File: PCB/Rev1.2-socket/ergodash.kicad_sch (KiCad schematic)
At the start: 183 parts, among them J1 5PIN, J2 Conn_01x03, J3 Conn_01x03, J4 GS3, J5 GS3, M1 Speaker, Q1 IRLML6344TRPbF, SW1 SW_PUSH, SW10 SW_PUSH, SW11 SW_PUSH, SW12 SW_PUSH, SW13 SW_PUSH, SW14 SW_PUSH, SW15 SW_PUSH, SW16 SW_PUSH, SW17 SW_PUSH, SW18 SW_PUSH, SW19 SW_PUSH, SW2 SW_PUSH, SW20 SW_PUSH, SW21 SW_PUSH, SW22 SW_PUSH, SW23 SW_PUSH, SW24 SW_PUSH, SW25 SW_PUSH, SW26 SW_PUSH, SW27 SW_PUSH, SW28 SW_PUSH, SW29 SW_Push, SW3 SW_PUSH, SW30 SW_PUSH, SW31 SW_PUSH, SW32 SW_PUSH, SW33 SW_PUSH, SW34 SW_PUSH, SW35 SW_PUSH, SW36 SW_PUSH, SW37 SW_Push, SW38 SW_PUSH, SW39 SW_PUSH, SW4 SW_PUSH, SW40 SW_PUSH, SW41 SW_PUSH, SW5 SW_PUSH, SW6 SW_PUSH, SW7 SW_PUSH, SW8 SW_PUSH, SW9 SW_PUSH, U1 HOLE, U2 HOLE, U3 ProMicro, U4 HOLE, U5 HOLE, U6 ProMicro, U7 HOLE, U8 HOLE, U9 HOLE

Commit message: Fix broken symbol resolution in KiCad 10 conversion
The first conversion silently dropped every custom symbol
(SW_PUSH, ProMicro, WS2812B, connectors, ...) because the legacy
schematic references libraries by their original nicknames while
KiCad only registered the cache library as ergodash-cache,
leaving those symbols pinless and disconnecting the switch matrix,
GND and more.

Split ergodash-cache.lib into per-nickname libraries under
library/ and register them in sym-lib-table, then re-import the
schematic. The exported netlist now matches the original
Rev1.2 netlist exactly (all 111 nets identical in membership).
Drop the legacy source files again now that the conversion is
verified.

Co-Authored-By: Claude Fable 5 <noreply@anthropic.com>
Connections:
- net Audio: now also U3.8 (C6), U6.8 (C6)
- net Backlight: now also U3.13 (B6), U6.13 (B6)
- net GND: now also J1.4, J1.5, J2.3 (Pin_3), J3.3 (Pin_3), J4.3 (G3), J5.3 (G3), M1.1 (GND), Q1.2 (S), SW29.2, SW37.2, U3.23 (GND), U3.3 (GND), U3.4 (GND), U6.23 (GND), U6.3 (GND), U6.4 (GND)
- net RBG: now also J2.2 (Pin_2), LED1.2 (DOUT), U3.1 (TX), U6.1 (TX)
- net RX: now also U3.2 (RX), U6.2 (RX)
- net VCC: now also J1.1, J2.1 (Pin_1), J3.1 (Pin_1), J4.1 (G1), J5.1 (G1), U3.21 (VCC), U6.21 (VCC)
- net col0: now also SW1.1, SW2.1, SW3.1, SW30.1, SW4.1, U3.20 (F4), U6.20 (F4)
- net col1: now also SW31.1, SW5.1, SW6.1, SW7.1, SW8.1, U3.19 (F5), U6.19 (F5)
- net col2: now also SW10.1, SW11.1, SW12.1, SW32.1, SW9.1, U3.18 (F6), U6.18 (F6)
- net col3: now also SW13.1, SW14.1, SW15.1, SW16.1, SW33.1, SW38.1, U3.17 (F7), U6.17 (F7)
- net col4: now also SW17.1, SW18.1, SW19.1, SW20.1, SW34.1, U3.16 (B1), U6.16 (B1)
- net col5: now also SW21.1, SW22.1, SW23.1, SW24.1, SW35.1, SW36.1, U3.15 (B3), U6.15 (B3)
- net col6: now also SW25.1, SW26.1, SW27.1, SW28.1, SW39.1, SW40.1, SW41.1, U3.14 (B2), U6.14 (B2)
- net row0: now also U3.7 (D4), U6.7 (D4)
- net row1: now also U3.9 (D7), U6.9 (D7)
- net row2: now also U3.10 (E6), U6.10 (E6)
- net row3: now also U3.11 (B4), U6.11 (B4)
- net row4: now also U3.12 (B5), U6.12 (B5)
- net rst: now also SW29.1, SW37.1, U3.22 (RST), U6.22 (RST)
- net scl: now also U3.5 (SCL), U6.5 (SCL), W1.2
- net sda/uart: now also J1.3, U3.6 (SDA), U6.6 (SDA)
- net xtradata: now also J1.2, J3.2 (Pin_2), LED12.4 (DIN), W1.1
- net at D1.2 (A): now also SW1.2
- net at D5.2 (A): now also SW5.2
- net at D9.2 (A): now also SW9.2
- net at D13.2 (A): now also SW13.2
- net at D17.2 (A): now also SW17.2
- net at D21.2 (A): now also SW21.2
- net at D25.2 (A): now also SW25.2
- net at D2.2 (A): now also SW2.2
- net at D6.2 (A): now also SW6.2
- net at D10.2 (A): now also SW10.2
- net at D14.2 (A): now also SW14.2
- net at D18.2 (A): now also SW18.2
- net at D22.2 (A): now also SW22.2
- net at D26.2 (A): now also SW26.2
- net at D27.2 (A): now also SW27.2
- net at D23.2 (A): now also SW23.2
- net at D19.2 (A): now also SW19.2
- net at D15.2 (A): now also SW15.2
- net at D11.2 (A): now also SW11.2
- net at D7.2 (A): now also SW7.2
- net at D3.2 (A): now also SW3.2
- net at D4.2 (A): now also SW4.2
- net at D8.2 (A): now also SW8.2
- net at D12.2 (A): now also SW12.2
- net at D16.2 (A): now also SW16.2
- net at D20.2 (A): now also SW20.2
- net at D24.2 (A): now also SW24.2
- net at D28.2 (A): now also SW28.2, SW39.2
- net at D29.2 (A): now also SW30.2
- net at D30.2 (A): now also SW31.2
- net at D31.2 (A): now also SW32.2
- net at D32.2 (A): now also SW33.2, SW38.2
- net at D33.2 (A): now also SW34.2
- net at D34.2 (A): now also SW35.2, SW36.2
- net at R10.2, R11.2, R12.2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: now also Q1.3 (D)
- net at R13.2: now also Q1.1 (G)
- net at D68.2 (A): now also SW40.2, SW41.2
- net at R40.2: now also M1.2 (Audio)
- new net: J4.2 (G2), LED1.1 (VCC), LED10.1 (VCC), LED11.1 (VCC), LED12.1 (VCC), LED2.1 (VCC), LED3.1 (VCC), LED4.1 (VCC), LED5.1 (VCC), LED6.1 (VCC), LED7.1 (VCC), LED8.1 (VCC), LED9.1 (VCC)
- new net: J5.2 (G2), LED1.3 (GND), LED10.3 (GND), LED11.3 (GND), LED12.3 (GND), LED2.3 (GND), LED3.3 (GND), LED4.3 (GND), LED5.3 (GND), LED6.3 (GND), LED7.3 (GND), LED8.3 (GND), LED9.3 (GND)
- new net: LED1.4 (DIN), LED2.2 (DOUT)
- new net: LED2.4 (DIN), LED3.2 (DOUT)
- new net: LED3.4 (DIN), LED4.2 (DOUT)
- new net: LED4.4 (DIN), LED5.2 (DOUT)
- new net: LED5.4 (DIN), LED6.2 (DOUT)
- new net: LED6.4 (DIN), LED7.2 (DOUT)
- new net: LED7.4 (DIN), LED8.2 (DOUT)
- new net: LED8.4 (DIN), LED9.2 (DOUT)
- new net: LED10.2 (DOUT), LED9.4 (DIN)
- new net: LED10.4 (DIN), LED11.2 (DOUT)
- new net: LED11.4 (DIN), LED12.2 (DOUT)

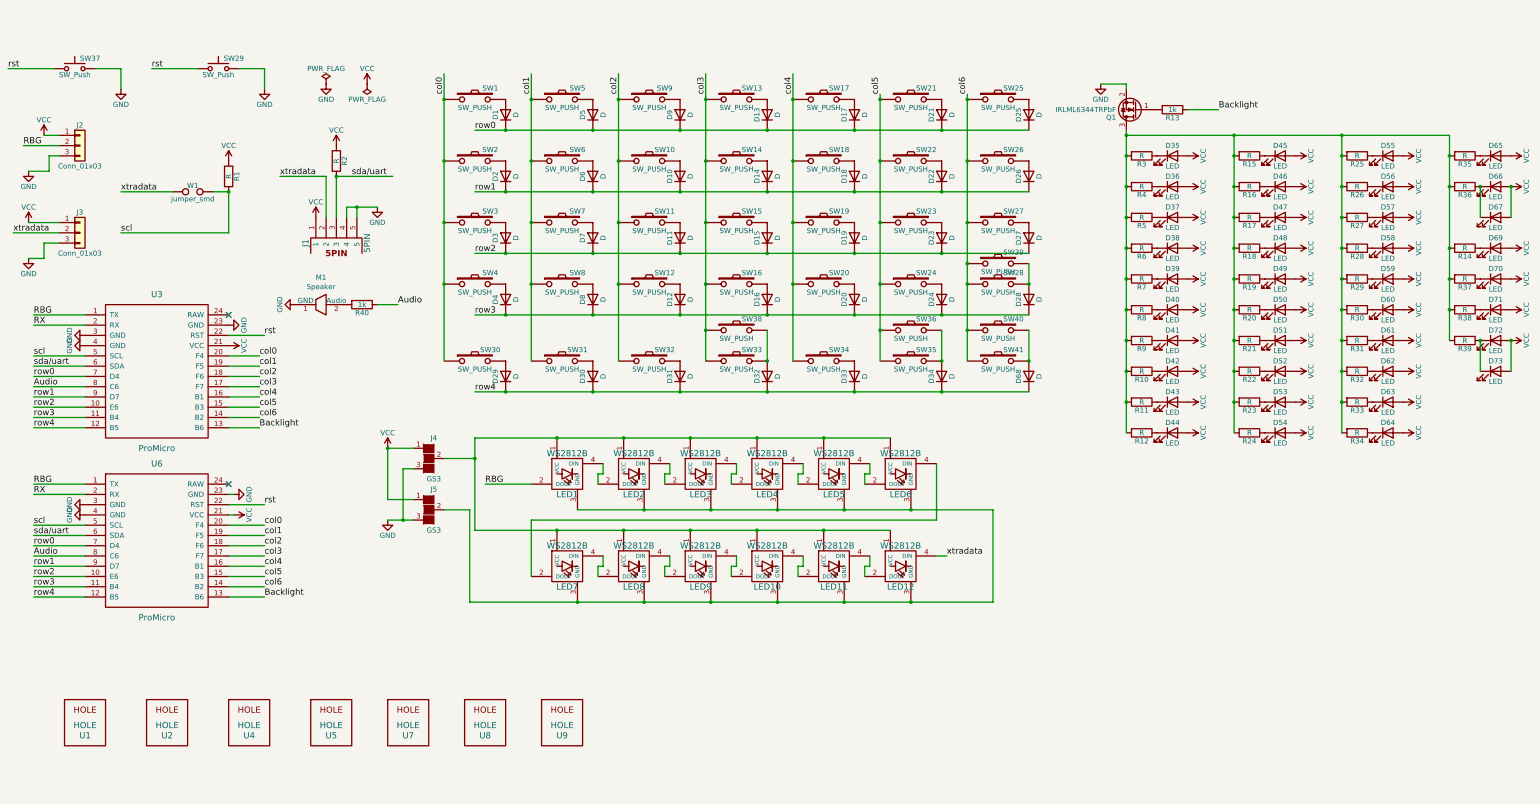
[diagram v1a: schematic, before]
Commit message: Remove all LED options from the schematic
Per the socket-version design policy: delete the WS2812B underglow
chain (LED1-12), per-switch 3mm backlight LEDs (D35-D67, D69-D73),
their 470 ohm resistors (R3-R12, R14-R39), the backlight driver
(Q1, R13) and the LED connectors/jumpers (J2-J5).

Verified by netlist diff against upstream Rev1.2: all 55 remaining
key-matrix/power/TRRS nets are identical in membership; the only
removed nets are LED-related. D68 (row4 matrix diode) and xtradata
(TRRS extra line) are intact.

Co-Authored-By: Claude Fable 5 <noreply@anthropic.com>
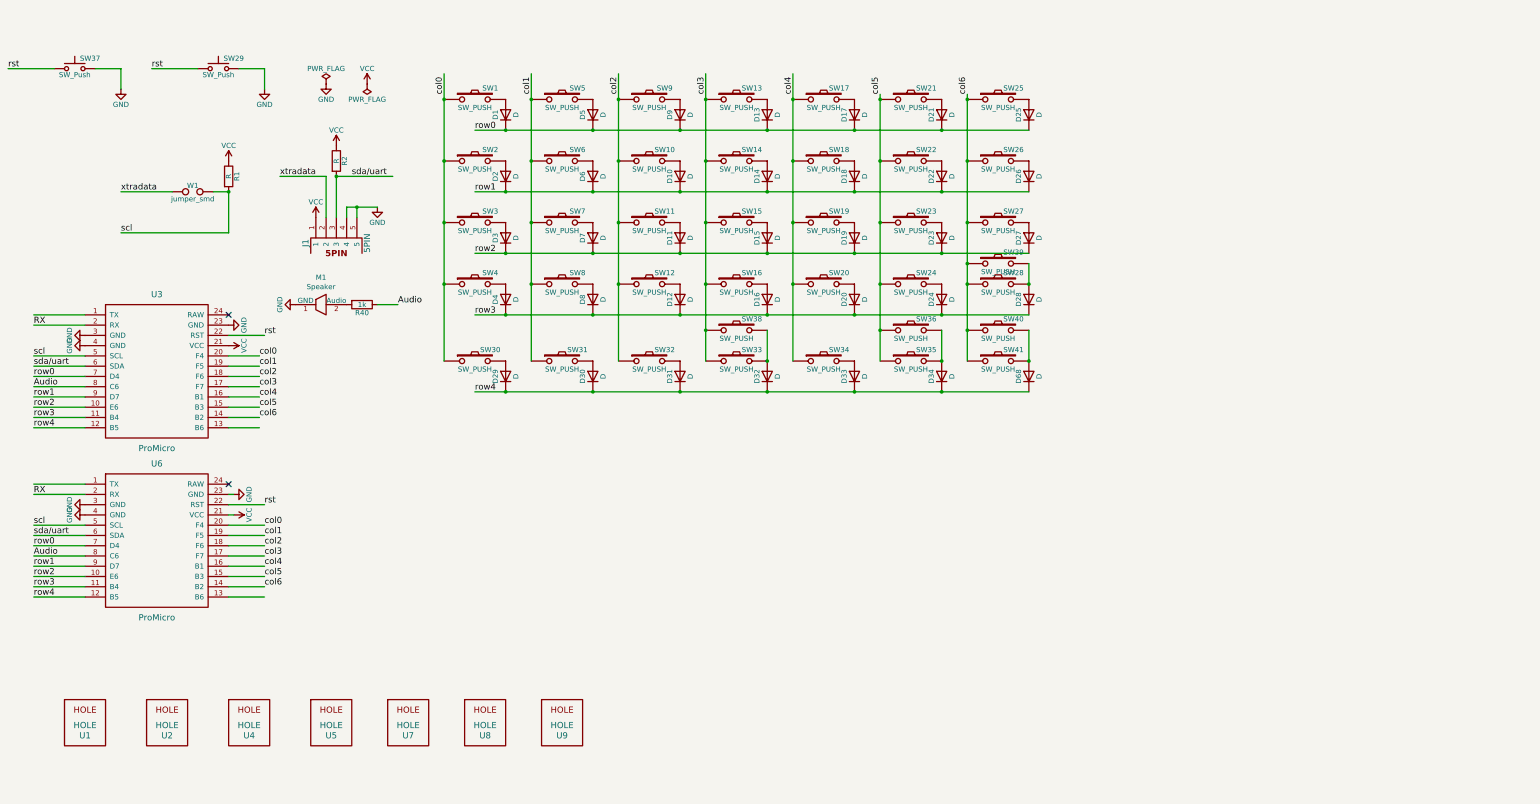
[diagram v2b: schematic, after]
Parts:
- removed D35, D36, D37, D38, D39, D40, D41, D42, D43, D44, D45, D46, D47, D48, D49, D50, D51, D52, D53, D54, D55, D56, D57, D58, D59, D60, D61, D62, D63, D64, D65, D66, D67, D69, D70, D71, D72, D73: LED, library:CHERRY_MX_LED2, symbol Device:LED
- removed J2, J3: Conn_01x03, library:conn3, symbol conn:Conn_01x03
- removed J4, J5: GS3, library:jumper2, symbol conn:GS3
- removed LED1, LED10, LED11, LED12, LED2, LED3, LED4, LED5, LED6, LED7, LED8, LED9: WS2812B, library:WS2812B-5, symbol ws2812b:WS2812B
- removed Q1: IRLML6344TRPbF, library:SOT-23_2, symbol transistors:BSS138
- removed R10, R11, R12, R14, R15, R16, R17, R18, R19, R20, R21, R22, R23, R24, R25, R26, R27, R28, R29, R3, R30, R31, R32, R33, R34, R35, R36, R37, R38, R39, R4, R5, R6, R7, R8, R9: R, library:Resistors_SMD_THT, symbol Device:R
- removed R13: 1k, library:Resistors_SMD_THT, symbol Device:R
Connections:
- net Backlight: no longer names the net of U3.13 (B6)
- net Backlight: no longer U6.13 (B6)
- net RBG: no longer names the net of U3.1 (TX)
- net RBG: no longer U6.1 (TX)

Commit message: Assign Kailh hotswap socket footprint to all key switches
Point the 39 SW_PUSH symbols at socket:SW_Hotswap_Kailh_MX_Plated
and fix the TRRS jack footprint reference to match the footprint
actually used on the board (trrs_jack2). Netlist unchanged.

Co-Authored-By: Claude Fable 5 <noreply@anthropic.com>
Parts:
- J1: footprint library:trrs_jack -> library:trrs_jack2
- SW1, SW10, SW11, SW12, SW13, SW14, SW15, SW16, SW17, SW18, SW19, SW2, SW20, SW21, SW22, SW23, SW24, SW25, SW26, SW27, SW28, SW3, SW30, SW31, SW32, SW33, SW34, SW35, SW36, SW38, SW39, SW4, SW40, SW41, SW5, SW6, SW7, SW8, SW9: footprint library:MX_ALPS -> socket:SW_Hotswap_Kailh_MX_Plated
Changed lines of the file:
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@@
 			)
 		)
-		(property "Footprint" "library:trrs_jack"
+		(property "Footprint" "library:trrs_jack2"
 			(at 96.52 60.96 0)
 			(hide yes)
@@
 			)
 		)
-		(property "Footprint" "library:MX_ALPS"
+		(property "Footprint" "socket:SW_Hotswap_Kailh_MX_Plated"
 			(at 129.54 26.67 0)
 			(hide yes)
@@
 			)
 		)
-		(property "Footprint" "library:MX_ALPS"
+		(property "Footprint" "socket:SW_Hotswap_Kailh_MX_Plated"
 			(at 151.13 26.67 0)
 			(hide yes)
@@
 			)
 		)
-		(property "Footprint" "library:MX_ALPS"
+		(property "Footprint" "socket:SW_Hotswap_Kailh_MX_Plated"
 			(at 172.72 26.67 0)
 			(hide yes)
@@
 			)
 		)
-		(property "Footprint" "library:MX_ALPS"
+		(property "Footprint" "socket:SW_Hotswap_Kailh_MX_Plated"
 			(at 194.31 26.67 0)
 			(hide yes)
@@
 			)
 		)
-		(property "Footprint" "library:MX_ALPS"
+		(property "Footprint" "socket:SW_Hotswap_Kailh_MX_Plated"
 			(at 215.9 26.67 0)
 			(hide yes)
@@
 			)
 		)
-		(property "Footprint" "library:MX_ALPS"
+		(property "Footprint" "socket:SW_Hotswap_Kailh_MX_Plated"
 			(at 237.49 26.67 0)
 			(hide yes)
@@
 			)
 		)
-		(property "Footprint" "library:MX_ALPS"
+		(property "Footprint" "socket:SW_Hotswap_Kailh_MX_Plated"
 			(at 259.08 26.67 0)
 			(hide yes)
@@
 			)
 		)
-		(property "Footprint" "library:MX_ALPS"
+		(property "Footprint" "socket:SW_Hotswap_Kailh_MX_Plated"
 			(at 129.54 41.91 0)
 			(hide yes)
@@
 			)
 		)
-		(property "Footprint" "library:MX_ALPS"
+		(property "Footprint" "socket:SW_Hotswap_Kailh_MX_Plated"
 			(at 151.13 41.91 0)
 			(hide yes)
@@
 			)
 		)
-		(property "Footprint" "library:MX_ALPS"
+		(property "Footprint" "socket:SW_Hotswap_Kailh_MX_Plated"
 			(at 172.72 41.91 0)
 			(hide yes)
@@
 			)
 		)
-		(property "Footprint" "library:MX_ALPS"
+		(property "Footprint" "socket:SW_Hotswap_Kailh_MX_Plated"
 			(at 194.31 41.91 0)
 			(hide yes)
@@
 			)
 		)
-		(property "Footprint" "library:MX_ALPS"
+		(property "Footprint" "socket:SW_Hotswap_Kailh_MX_Plated"
 			(at 215.9 41.91 0)
 			(hide yes)
@@
 			)
 		)
-		(property "Footprint" "library:MX_ALPS"
+		(property "Footprint" "socket:SW_Hotswap_Kailh_MX_Plated"
 			(at 237.49 41.91 0)
 			(hide yes)
@@
 			)
 		)
-		(property "Footprint" "library:MX_ALPS"
+		(property "Footprint" "socket:SW_Hotswap_Kailh_MX_Plated"
 			(at 259.08 41.91 0)
 			(hide yes)
@@
 			)
 		)
-		(property "Footprint" "library:MX_ALPS"
+		(property "Footprint" "socket:SW_Hotswap_Kailh_MX_Plated"
 			(at 259.08 57.15 0)
 			(hide yes)
@@
 			)
 		)
-		(property "Footprint" "library:MX_ALPS"
+		(property "Footprint" "socket:SW_Hotswap_Kailh_MX_Plated"
 			(at 237.49 57.15 0)
 			(hide yes)
@@
 			)
 		)
-		(property "Footprint" "library:MX_ALPS"
+		(property "Footprint" "socket:SW_Hotswap_Kailh_MX_Plated"
 			(at 215.9 57.15 0)
 			(hide yes)
@@
 			)
 		)
-		(property "Footprint" "library:MX_ALPS"
+		(property "Footprint" "socket:SW_Hotswap_Kailh_MX_Plated"
 			(at 194.31 57.15 0)
 			(hide yes)
@@
 			)
 		)
-		(property "Footprint" "library:MX_ALPS"
+		(property "Footprint" "socket:SW_Hotswap_Kailh_MX_Plated"
 			(at 172.72 57.15 0)
 			(hide yes)
@@
 			)
 		)
-		(property "Footprint" "library:MX_ALPS"
+		(property "Footprint" "socket:SW_Hotswap_Kailh_MX_Plated"
 			(at 151.13 57.15 0)
 			(hide yes)
@@
 			)
 		)
-		(property "Footprint" "library:MX_ALPS"
+		(property "Footprint" "socket:SW_Hotswap_Kailh_MX_Plated"
 			(at 129.54 57.15 0)
 			(hide yes)
@@
 			)
 		)
-		(property "Footprint" "library:MX_ALPS"
+		(property "Footprint" "socket:SW_Hotswap_Kailh_MX_Plated"
 			(at 129.54 72.39 0)
 			(hide yes)
@@
 			)
 		)
-		(property "Footprint" "library:MX_ALPS"
+		(property "Footprint" "socket:SW_Hotswap_Kailh_MX_Plated"
 			(at 151.13 72.39 0)
 			(hide yes)
@@
 			)
 		)
-		(property "Footprint" "library:MX_ALPS"
+		(property "Footprint" "socket:SW_Hotswap_Kailh_MX_Plated"
 			(at 172.72 72.39 0)
 			(hide yes)
@@
 			)
 		)
-		(property "Footprint" "library:MX_ALPS"
+		(property "Footprint" "socket:SW_Hotswap_Kailh_MX_Plated"
 			(at 194.31 72.39 0)
 			(hide yes)
@@
 			)
 		)
-		(property "Footprint" "library:MX_ALPS"
+		(property "Footprint" "socket:SW_Hotswap_Kailh_MX_Plated"
 			(at 215.9 72.39 0)
 			(hide yes)
@@
 			)
 		)
-		(property "Footprint" "library:MX_ALPS"
+		(property "Footprint" "socket:SW_Hotswap_Kailh_MX_Plated"
 			(at 237.49 72.39 0)
 			(hide yes)
@@
 			)
 		)
-		(property "Footprint" "library:MX_ALPS"
+		(property "Footprint" "socket:SW_Hotswap_Kailh_MX_Plated"
 			(at 259.08 72.39 0)
 			(hide yes)
@@
 			)
 		)
-		(property "Footprint" "library:MX_ALPS"
+		(property "Footprint" "socket:SW_Hotswap_Kailh_MX_Plated"
 			(at 129.54 91.44 0)
 			(hide yes)
@@
 			)
 		)
-		(property "Footprint" "library:MX_ALPS"
+		(property "Footprint" "socket:SW_Hotswap_Kailh_MX_Plated"
 			(at 151.13 91.44 0)
 			(hide yes)
@@
 			)
 		)
-		(property "Footprint" "library:MX_ALPS"
+		(property "Footprint" "socket:SW_Hotswap_Kailh_MX_Plated"
 			(at 172.72 91.44 0)
 			(hide yes)
@@
 			)
 		)
-		(property "Footprint" "library:MX_ALPS"
+		(property "Footprint" "socket:SW_Hotswap_Kailh_MX_Plated"
 			(at 194.31 91.44 0)
 			(hide yes)
@@
 			)
 		)
-		(property "Footprint" "library:MX_ALPS"
+		(property "Footprint" "socket:SW_Hotswap_Kailh_MX_Plated"
 			(at 215.9 91.44 0)
 			(hide yes)
@@
 			)
 		)
-		(property "Footprint" "library:MX_ALPS"
+		(property "Footprint" "socket:SW_Hotswap_Kailh_MX_Plated"
 			(at 237.49 91.44 0)
 			(hide yes)
@@
 			)
 		)
-		(property "Footprint" "library:MX_ALPS"
+		(property "Footprint" "socket:SW_Hotswap_Kailh_MX_Plated"
 			(at 237.49 83.82 0)
 			(hide yes)
@@
 			)
 		)
-		(property "Footprint" "library:MX_ALPS"
+		(property "Footprint" "socket:SW_Hotswap_Kailh_MX_Plated"
 			(at 194.31 83.82 0)
 			(hide yes)
@@
 			)
 		)
-		(property "Footprint" "library:MX_ALPS"
+		(property "Footprint" "socket:SW_Hotswap_Kailh_MX_Plated"
 			(at 259.08 91.44 0)
 			(hide yes)
@@
 			)
 		)
-		(property "Footprint" "library:MX_ALPS"
+		(property "Footprint" "socket:SW_Hotswap_Kailh_MX_Plated"
 			(at 259.08 83.82 0)
 			(hide yes)
@@
 			)
 		)
-		(property "Footprint" "library:MX_ALPS"
+		(property "Footprint" "socket:SW_Hotswap_Kailh_MX_Plated"
 			(at 259.08 67.31 0)
 			(hide yes)

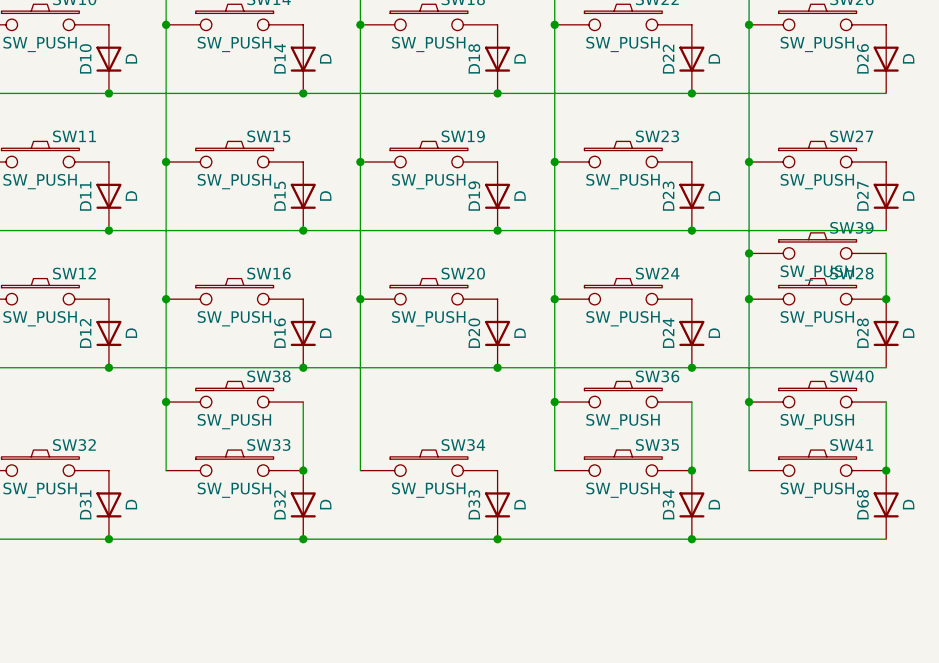
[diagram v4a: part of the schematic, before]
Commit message: Route the left board and drop alternative key layouts
Manual routing of the key matrix done in the GUI. Remove the
alternative-position switches (SW36, SW38, SW39, SW41) from the
schematic, keeping SW40 as the only 2U key, and delete the now
orphaned 2U stabilizer at the old SW36 position, which also
resolves the hole clearance conflict with the SW35 socket pad.
Re-apply the U6 on_board=no exclusion that was lost to a
concurrent eeschema save.

Co-Authored-By: Claude Fable 5 <noreply@anthropic.com>
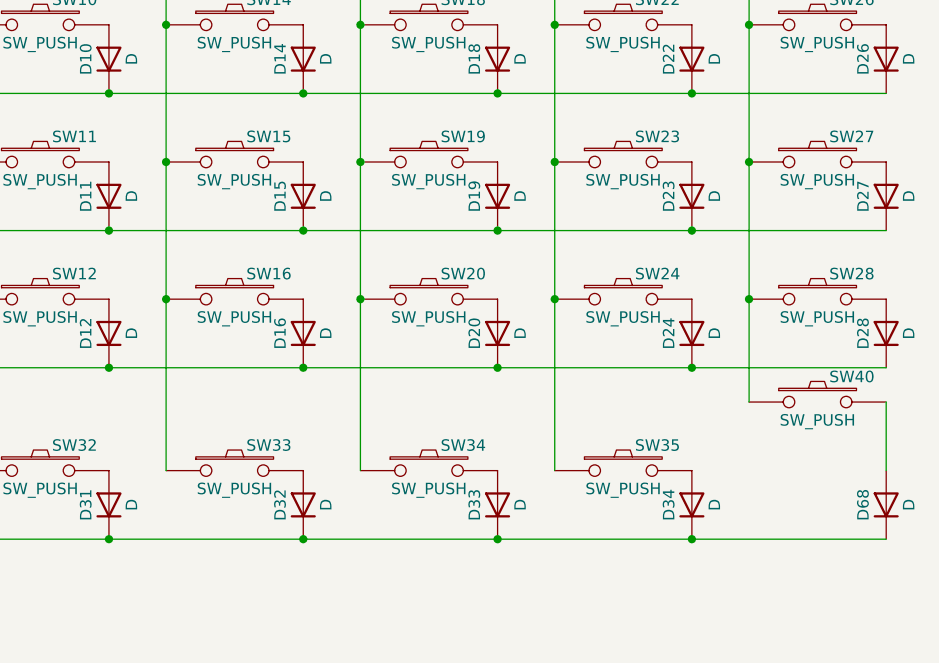
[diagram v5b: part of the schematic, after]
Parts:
- removed SW36, SW38, SW39, SW41: SW_PUSH, socket:SW_Hotswap_Kailh_MX_Plated, symbol ergodash:SW_PUSH
